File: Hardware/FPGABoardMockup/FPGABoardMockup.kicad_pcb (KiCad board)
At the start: 2 copper layers, 104 x 66 mm, 16 parts, among them J1 Conn_02x14_Odd_Even, J2 Conn_02x11_Counter_Clockwise, J3 Barrel_Jack, J4 Conn_02x05_Counter_Clockwise, J5 USB_B_Mini, J6 Conn_02x05_Counter_Clockwise, J7 Conn_02x14_Odd_Even, J8 Conn_02x11_Counter_Clockwise, SW1 SW_Push, SW2 SW_Push, SW3 SW_Push, SW4 SW_Push

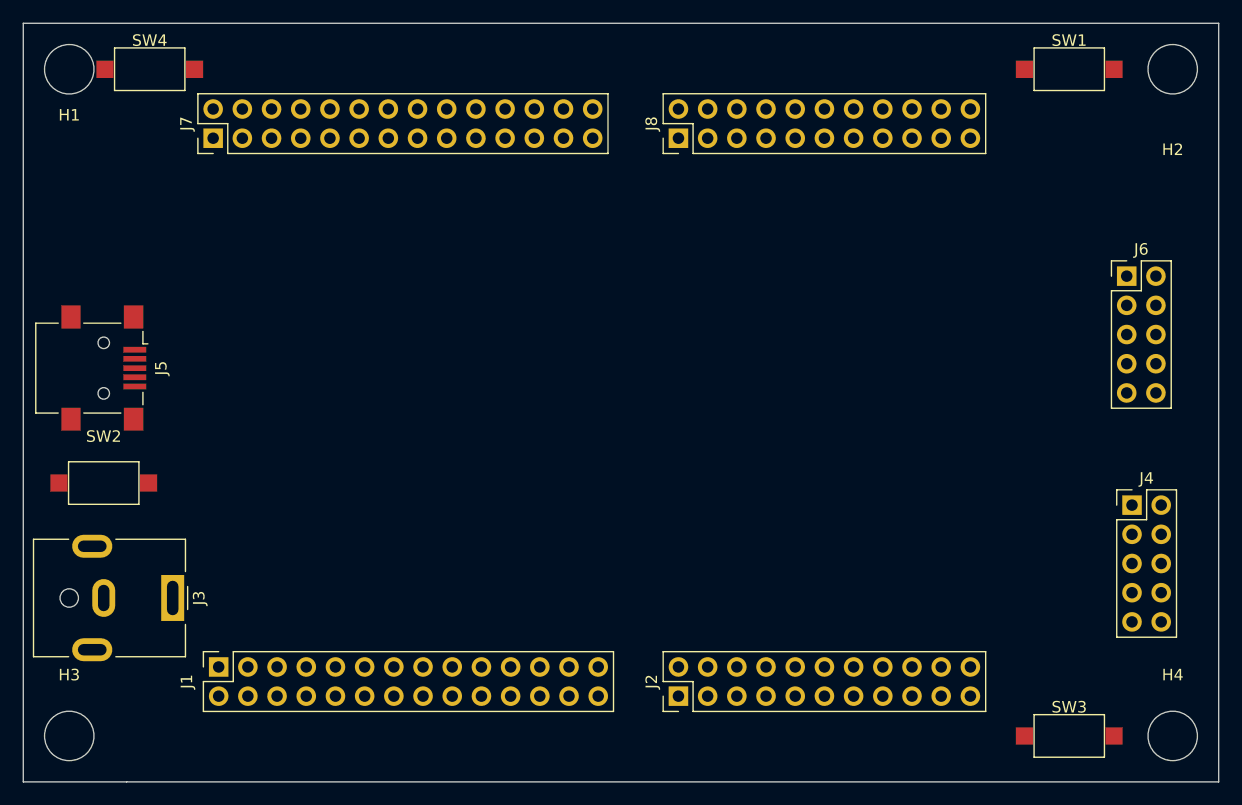
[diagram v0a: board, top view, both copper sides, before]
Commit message: finished mechanical overview design
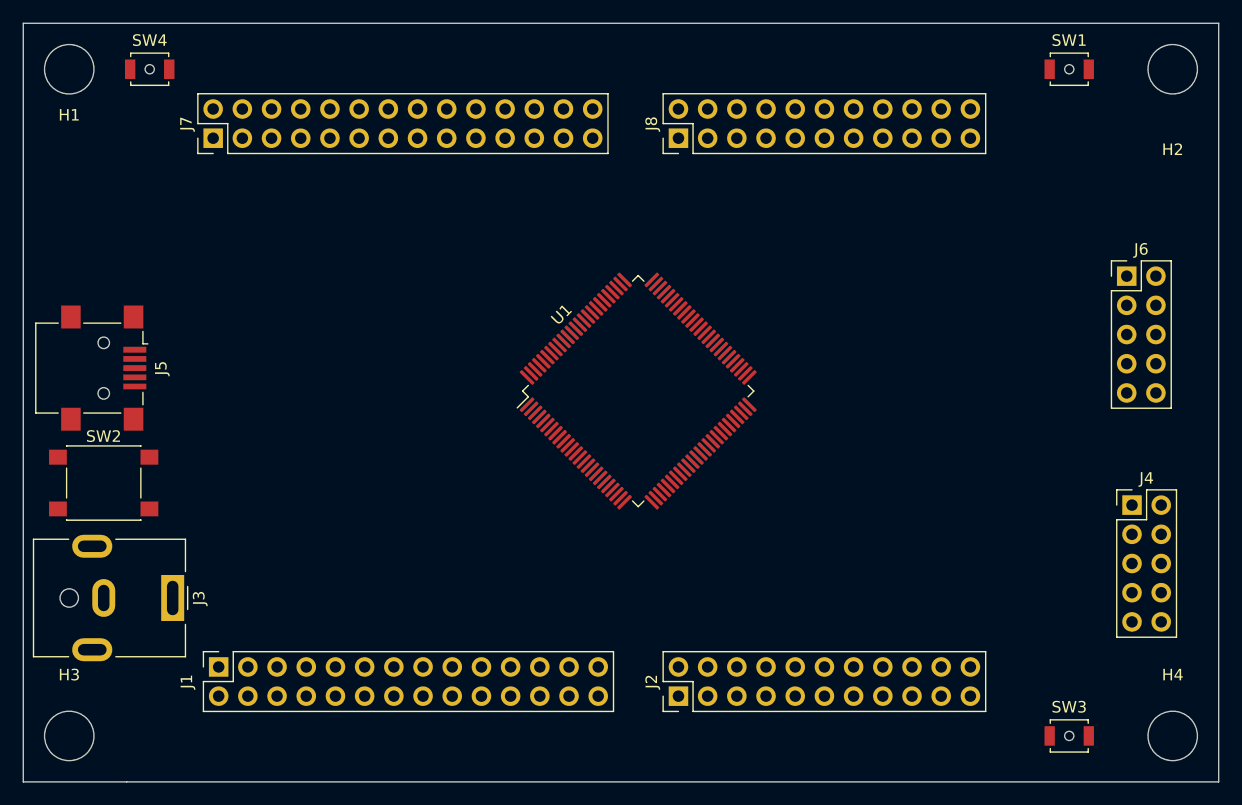
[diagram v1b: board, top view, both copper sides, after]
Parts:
- added U1: EPM240T100, Package_QFP:LQFP-100_14x14mm_P0.5mm, F.Cu at (154.5, 82.0)
- SW1, SW3, SW4: footprint Button_Switch_SMD:SW_SPST_CK_RS282G05A3 -> Button_Switch_SMD:SW_SPST_B3U-1000P-B
- SW2: footprint Button_Switch_SMD:SW_SPST_CK_RS282G05A3 -> Button_Switch_SMD:SW_SPST_PTS645
